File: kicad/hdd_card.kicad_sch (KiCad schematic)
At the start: 23 parts, among them J1 POISK, J2 ICSP, J3 SDCARD, J4 UART, U1 28C256, U2 74LS245, U3 28C256, U4 PIC18F47Q10-xP, U5 74LS00, U6 74LS32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

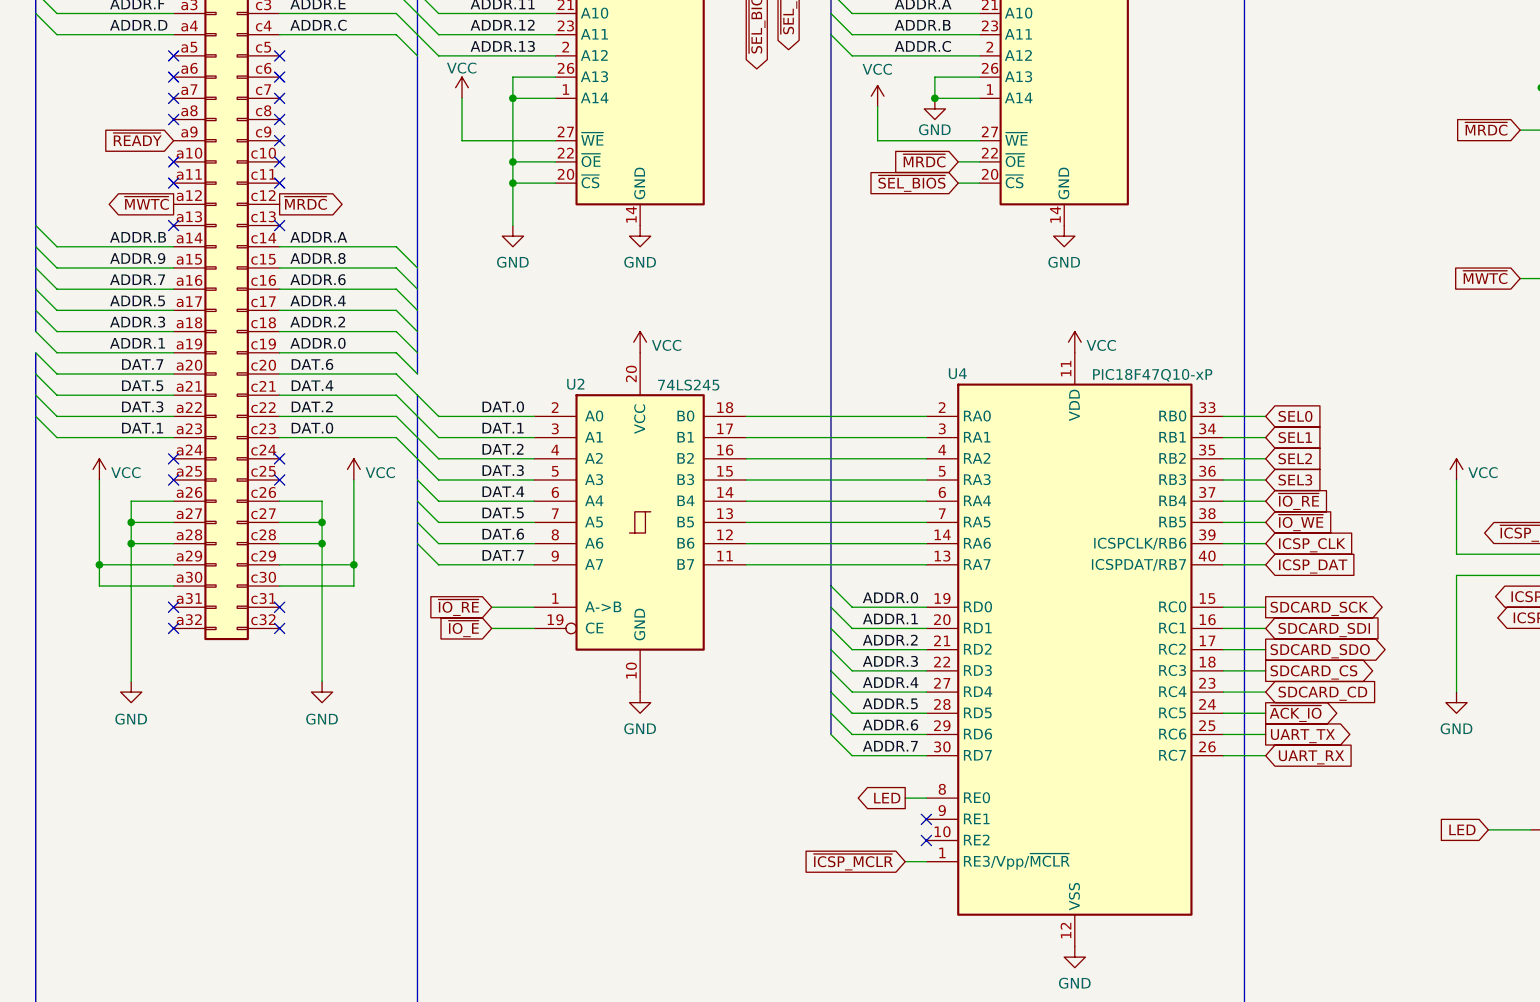
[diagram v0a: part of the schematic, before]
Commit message: IRQ_DONE <-> INTR5
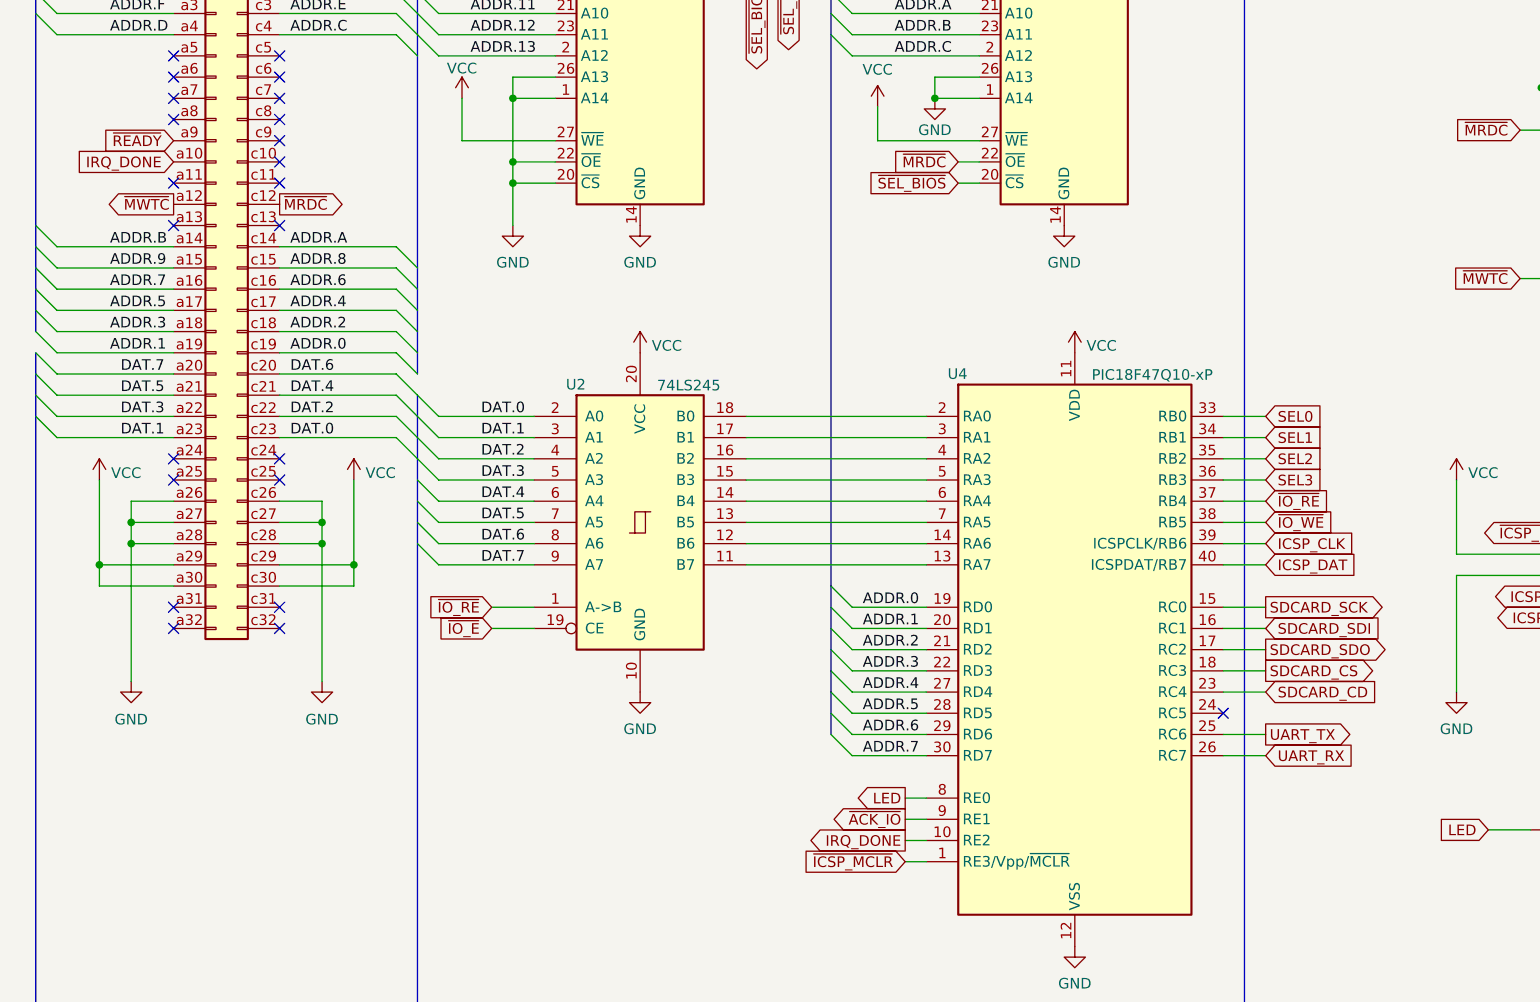
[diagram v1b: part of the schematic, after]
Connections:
- net ~{ACK_IO}: now also U4.9 (RE1); no longer U4.24 (RC5)
- net IRQ_DONE: now reaches U4.10 (RE2)
- net IRQ_DONE: now also J1.a10 (Pin_a10)
- no-connect marks 33 -> 31

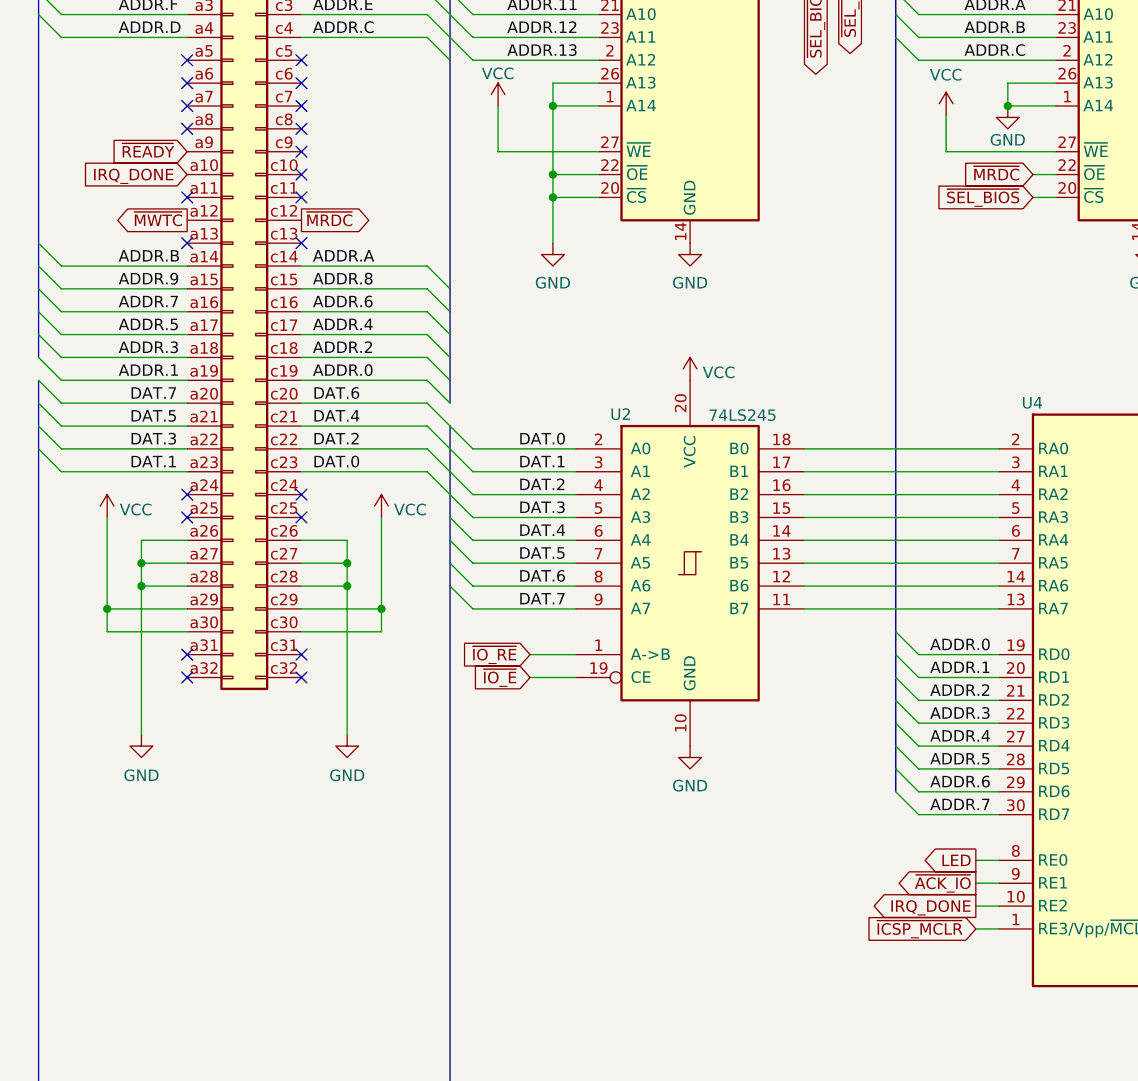
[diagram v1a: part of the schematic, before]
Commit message: Request complete interrupt. Multi-sector IO data.
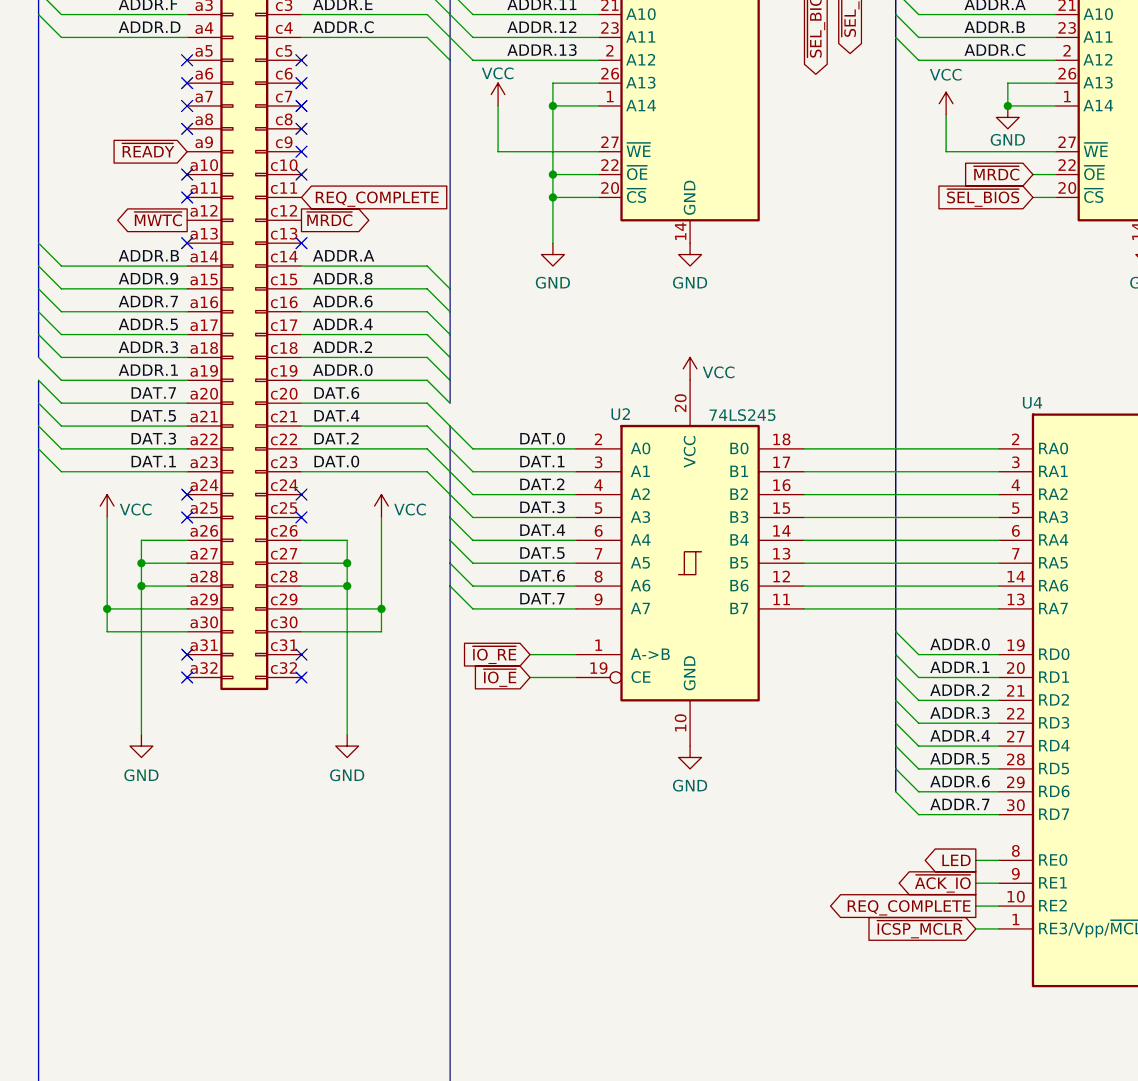
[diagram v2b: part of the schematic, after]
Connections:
- net REQ_COMPLETE: now reaches J1.c11 (Pin_c11)
- net REQ_COMPLETE: now also U4.10 (RE2)
- net IRQ_DONE: no longer names the net of J1.a10 (Pin_a10)
- net IRQ_DONE: no longer U4.10 (RE2)
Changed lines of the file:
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@@
   (no_connect (at 34.29 67.31))
   (no_connect (at 46.99 125.73))
-  (no_connect (at 46.99 74.93))
+  (no_connect (at 34.29 72.39))
   (no_connect (at 262.89 121.92))
   (no_connect (at 262.89 119.38))
@@
     )
   )
+  (global_label "REQ_COMPLETE" (shape input) (at 46.99 74.93 0) (fields_autoplaced)
+    (effects (font (size 1.27 1.27)) (justify left))
+    (property "Intersheet References" "${INTERSHEET_REFS}" (id 0) (at 63.736 75.0094 0)
+      (effects (font (size 1.27 1.27)) (justify left) hide)
+    )
+  )
   (global_label "SDCARD_CD" (shape input) (at 165.1 135.89 0) (fields_autoplaced)
     (effects (font (size 1.27 1.27)) (justify left))
@@
     )
   )
-  (global_label "IRQ_DONE" (shape output) (at 121.92 153.67 180) (fields_autoplaced)
-    (effects (font (size 1.27 1.27)) (justify right))
-    (property "Intersheet References" "${INTERSHEET_REFS}" (id 0) (at 110.254 153.5906 0)
+  (global_label "REQ_COMPLETE" (shape output) (at 121.92 153.67 180) (fields_autoplaced)
+    (effects (font (size 1.27 1.27)) (justify right))
+    (property "Intersheet References" "${INTERSHEET_REFS}" (id 0) (at 105.174 153.5906 0)
       (effects (font (size 1.27 1.27)) (justify right) hide)
     )
@@
     )
   )
-  (global_label "IRQ_DONE" (shape input) (at 34.29 72.39 180) (fields_autoplaced)
-    (effects (font (size 1.27 1.27)) (justify right))
-    (property "Intersheet References" "${INTERSHEET_REFS}" (id 0) (at 22.624 72.4694 0)
-      (effects (font (size 1.27 1.27)) (justify right) hide)
-    )
-  )

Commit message: SEL4
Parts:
- added JP1: IRQ 2, Connector_PinHeader_2.54mm:PinHeader_1x02_P2.54mm_Vertical, symbol Jumper:Jumper_2_Open
- added JP2: IRQ 3, Connector_PinHeader_2.54mm:PinHeader_1x02_P2.54mm_Vertical, symbol Jumper:Jumper_2_Open
- added JP3: IRQ 4, Connector_PinHeader_2.54mm:PinHeader_1x02_P2.54mm_Vertical, symbol Jumper:Jumper_2_Open
- added JP4: IRQ 5, Connector_PinHeader_2.54mm:PinHeader_1x02_P2.54mm_Vertical, symbol Jumper:Jumper_2_Open
- added JP5: IRQ 7, Connector_PinHeader_2.54mm:PinHeader_1x02_P2.54mm_Vertical, symbol Jumper:Jumper_2_Open
- D1: footprint (none) -> LED_THT:LED_D5.0mm
- J2, J4: footprint (none) -> Connector_PinHeader_2.54mm:PinHeader_1x06_P2.54mm_Vertical
- J3: footprint (none) -> Connector_PinHeader_2.54mm:PinHeader_1x08_P2.54mm_Vertical
- R1, R2, R3, R4: footprint (none) -> Resistor_THT:R_Axial_DIN0207_L6.3mm_D2.5mm_P7.62mm_Horizontal
- U1, U3: footprint (none) -> Package_DIP:DIP-28_W15.24mm
- U2: footprint (none) -> Package_DIP:DIP-20_W7.62mm
- U5, U6, U7, U8: footprint (none) -> Package_DIP:DIP-14_W7.62mm
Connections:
- net REQ_COMPLETE: now also JP1.2 (B), JP2.2 (B), JP3.2 (B), JP4.2 (B), JP5.2 (B); no longer J1.c11 (Pin_c11)
- net SDCARD_CD: now also U4.24 (RC5); no longer U4.23 (RC4)
- net SEL4: now reaches U1.16 (D4)
- net SEL4: now also U4.23 (RC4)
- net INTR5: now reaches J1.a10 (Pin_a10)
- net INTR5: now also JP4.1 (A)
- net INTR3: now reaches J1.a11 (Pin_a11)
- net INTR3: now also JP2.1 (A)
- net INTR4: now reaches J1.c10 (Pin_c10)
- net INTR4: now also JP3.1 (A)
- net INTR7: now reaches J1.c9 (Pin_c9)
- net INTR7: now also JP5.1 (A)
- new net INTR2: J1.c11 (Pin_c11), JP1.1 (A)
- no-connect marks 31 -> 25

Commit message: WIP
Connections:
- net SDCARD_CS: now also U4.36 (RB3); no longer U4.18 (RC3)
- net SDCARD_SCK: now also U4.33 (RB0); no longer U4.15 (RC0)
- net SDCARD_SDI: now also U4.34 (RB1); no longer U4.16 (RC1)
- net SDCARD_SDO: now also U4.35 (RB2); no longer U4.17 (RC2)
- net SEL0: now also U4.15 (RC0); no longer U4.33 (RB0)
- net SEL1: now also U4.16 (RC1); no longer U4.34 (RB1)
- net SEL2: now also U4.17 (RC2); no longer U4.35 (RB2)
- net SEL3: now also U4.18 (RC3); no longer U4.36 (RB3)
